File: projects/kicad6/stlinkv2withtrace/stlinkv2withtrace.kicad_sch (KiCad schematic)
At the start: 7 parts, among them J3 STLinkV2, U1 YAAJ_BluePill_Part_Like

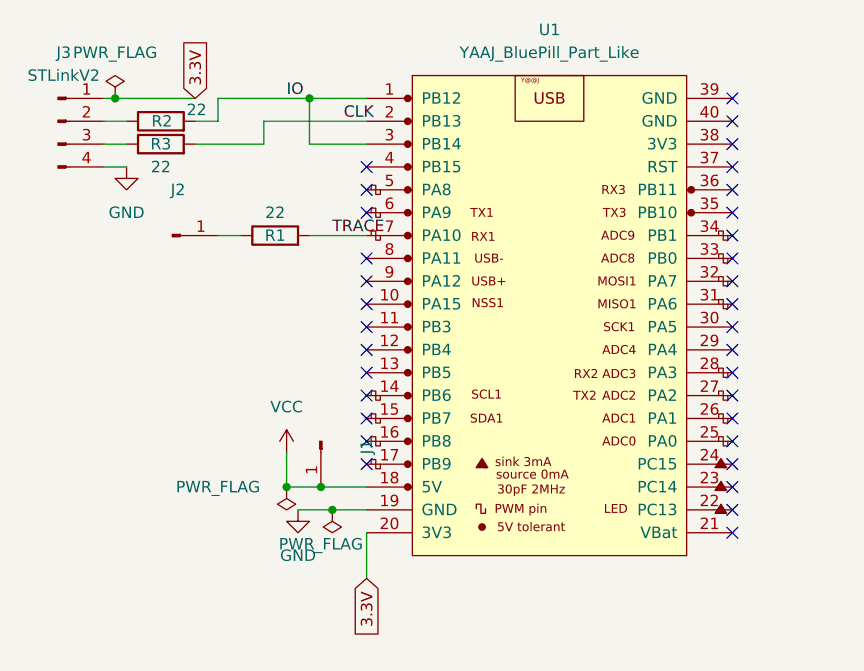
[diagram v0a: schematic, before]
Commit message: Add stlink v2 diy programmer
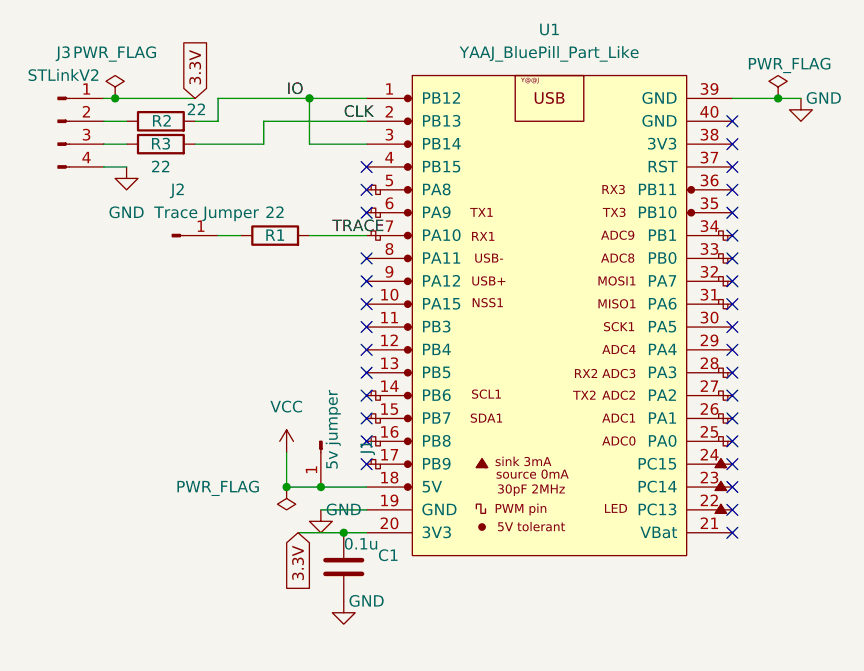
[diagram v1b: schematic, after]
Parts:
- added C1: 0.1u, Capacitor_THT:C_Axial_L3.8mm_D2.6mm_P7.50mm_Horizontal, symbol Device:C
- J1: value (none) -> 5v jumper
- J2: value (none) -> Trace Jumper; footprint (none) -> Connector_PinSocket_2.54mm:PinSocket_1x01_P2.54mm_Vertical
- J3: footprint (none) -> Connector_PinSocket_2.54mm:PinSocket_1x04_P2.54mm_Horizontal
- R1, R2, R3: footprint (none) -> Resistor_THT:R_Axial_DIN0207_L6.3mm_D2.5mm_P7.62mm_Horizontal
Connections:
- net 3.3V: now also C1.1
- net GND: now also U1.39 (GND), C1.2
- no-connect marks 33 -> 32
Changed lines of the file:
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@@
     (company "Amitesh Singh")
   )
-  (junction (at 116.84 110.49) (diameter 0) (color 0 0 0 0)
+  (junction (at 166.37 64.77) (diameter 0) (color 0 0 0 0)
   )
   (junction (at 114.3 64.77) (diameter 0) (color 0 0 0 0)
   )
   (junction (at 111.76 107.95) (diameter 0) (color 0 0 0 0)
+  )
+  (junction (at 118.11 113.03) (diameter 0) (color 0 0 0 0)
   )
   (junction (at 92.71 64.77) (diameter 0) (color 0 0 0 0)
@@
   (no_connect (at 120.65 77.47))
   (no_connect (at 120.65 82.55))
+  (no_connect (at 161.29 69.85))
   (no_connect (at 161.29 113.03))
   (no_connect (at 161.29 110.49))
@@
   (no_connect (at 161.29 85.09))
   (no_connect (at 161.29 72.39))
-  (no_connect (at 161.29 69.85))
   (no_connect (at 161.29 67.31))
-  (no_connect (at 161.29 64.77))
   (no_connect (at 161.29 77.47))
   (no_connect (at 161.29 80.01))
@@
     (stroke (width 0) (type default) (color 0 0 0 0))
   )
-  (wire (pts (xy 120.65 118.11) (xy 120.65 113.03))
+  (wire (pts (xy 115.57 110.49) (xy 120.65 110.49))
     (stroke (width 0) (type default) (color 0 0 0 0))
   )
@@
     (stroke (width 0) (type default) (color 0 0 0 0))
   )
+  (wire (pts (xy 161.29 64.77) (xy 166.37 64.77))
+    (stroke (width 0) (type default) (color 0 0 0 0))
+  )
   (wire (pts (xy 114.3 64.77) (xy 114.3 69.85))
     (stroke (width 0) (type default) (color 0 0 0 0))
@@
     (stroke (width 0) (type default) (color 0 0 0 0))
   )
-  (wire (pts (xy 113.03 110.49) (xy 116.84 110.49))
+  (wire (pts (xy 166.37 64.77) (xy 168.91 64.77))
+    (stroke (width 0) (type default) (color 0 0 0 0))
+  )
+  (wire (pts (xy 118.11 113.03) (xy 113.03 113.03))
     (stroke (width 0) (type default) (color 0 0 0 0))
   )
@@
     (stroke (width 0) (type default) (color 0 0 0 0))
   )
-  (wire (pts (xy 116.84 110.49) (xy 120.65 110.49))
+  (wire (pts (xy 120.65 113.03) (xy 118.11 113.03))
     (stroke (width 0) (type default) (color 0 0 0 0))
   )
@@
     )
   )
-  (global_label "3.3V" (shape input) (at 120.65 118.11 270) (fields_autoplaced)
+  (global_label "3.3V" (shape input) (at 113.03 113.03 270) (fields_autoplaced)
     (effects (font (size 1.27 1.27)) (justify right))
-    (property "Intersheet References" "${INTERSHEET_REFS}" (id 0) (at 120.5706 124.6355 90)
+    (property "Intersheet References" "${INTERSHEET_REFS}" (id 0) (at 112.9506 119.5555 90)
       (effects (font (size 1.27 1.27)) (justify right) hide)
     )
@@
     (pin "1")
   )
+  (symbol (lib_id "Device:C") (at 118.11 116.84 0) (unit 1)
+    (in_bom yes) (on_board yes)
+    (property "Reference" "C1" (id 0) (at 121.92 115.5699 0)
+      (effects (font (size 1.27 1.27)) (justify left))
+    )
+    (property "Value" "0.1u" (id 1) (at 118.11 114.3 0)
+      (effects (font (size 1.27 1.27)) (justify left))
+    )
+    (property "Footprint" "Capacitor_THT:C_Axial_L3.8mm_D2.6mm_P7.50mm_Horizontal" (id 2) (at 119.0752 120.65 0)
+      (effects (font (size 1.27 1.27)) hide)
+    )
+    (property "Datasheet" "~" (id 3) (at 118.11 116.84 0)
+      (effects (font (size 1.27 1.27)) hide)
+    )
+    (pin "1")
+    (pin "2")
+  )
   (symbol (lib_id "Device:R") (at 110.49 80.01 90) (unit 1)
     (in_bom yes) (on_board yes)
     (property "Reference" "R1" (id 0) (at 110.49 80.01 90))
     (property "Value" "22" (id 1) (at 110.49 77.47 90))
-    (property "Footprint" "" (id 2) (at 110.49 81.788 90)
+    (property "Footprint" "Resistor_THT:R_Axial_DIN0207_L6.3mm_D2.5mm_P7.62mm_Horizontal" (id 2) (at 110.49 81.788 90)
       (effects (font (size 1.27 1.27)) hide)
     )
@@
     (pin "1")
     (pin "2")
+  )
+  (symbol (lib_id "power:GND") (at 118.11 120.65 0) (unit 1)
+    (in_bom yes) (on_board yes)
+    (property "Reference" "#PWR04" (id 0) (at 118.11 127 0)
+      (effects (font (size 1.27 1.27)) hide)
+    )
+    (property "Value" "GND" (id 1) (at 120.65 120.65 0))
+    (property "Footprint" "" (id 2) (at 118.11 120.65 0)
+      (effects (font (size 1.27 1.27)) hide)
+    )
+    (property "Datasheet" "" (id 3) (at 118.11 120.65 0)
+      (effects (font (size 1.27 1.27)) hide)
+    )
+    (pin "1")
   )
   (symbol (lib_id "YAAJ_BlackPill_SWD_Breakout:YAAJ_BluePill_Part_Like") (at 140.97 87.63 0) (unit 1)
@@
       (effects (font (size 1.27 1.27)) (justify left))
     )
-    (property "Footprint" "" (id 2) (at 97.79 69.088 90)
+    (property "Footprint" "Resistor_THT:R_Axial_DIN0207_L6.3mm_D2.5mm_P7.62mm_Horizontal" (id 2) (at 97.79 69.088 90)
       (effects (font (size 1.27 1.27)) hide)
     )
@@
     (in_bom yes) (on_board yes)
     (property "Reference" "J1" (id 0) (at 120.65 103.505 0))
-    (property "Value" "" (id 1) (at 116.84 101.6 0))
+    (property "Value" "5v jumper" (id 1) (at 116.84 101.6 0))
     (property "Footprint" "Connector_PinSocket_2.54mm:PinSocket_1x01_P2.54mm_Vertical" (id 2) (at 115.57 102.87 0)
       (effects (font (size 1.27 1.27)) hide)
     )
     (property "Datasheet" "~" (id 3) (at 115.57 102.87 0)
+      (effects (font (size 1.27 1.27)) hide)
+    )
+    (pin "1")
+  )
+  (symbol (lib_id "power:GND") (at 115.57 110.49 0) (unit 1)
+    (in_bom yes) (on_board yes)
+    (property "Reference" "#PWR05" (id 0) (at 115.57 116.84 0)
+      (effects (font (size 1.27 1.27)) hide)
+    )
+    (property "Value" "GND" (id 1) (at 118.11 110.49 0))
+    (property "Footprint" "" (id 2) (at 115.57 110.49 0)
+      (effects (font (size 1.27 1.27)) hide)
+    )
+    (property "Datasheet" "" (id 3) (at 115.57 110.49 0)
       (effects (font (size 1.27 1.27)) hide)
     )
@@
     (in_bom yes) (on_board yes)
     (property "Reference" "J2" (id 0) (at 99.695 74.93 0))
-    (property "Value" "" (id 1) (at 102.87 77.47 0))
-    (property "Footprint" "" (id 2) (at 99.06 80.01 0)
+    (property "Value" "Trace Jumper" (id 1) (at 102.87 77.47 0))
+    (property "Footprint" "Connector_PinSocket_2.54mm:PinSocket_1x01_P2.54mm_Vertical" (id 2) (at 99.06 80.01 0)
       (effects (font (size 1.27 1.27)) hide)
     )
@@
     (property "Reference" "R3" (id 0) (at 97.79 69.85 90))
     (property "Value" "22" (id 1) (at 97.79 72.39 90))
-    (property "Footprint" "" (id 2) (at 97.79 71.628 90)
+    (property "Footprint" "Resistor_THT:R_Axial_DIN0207_L6.3mm_D2.5mm_P7.62mm_Horizontal" (id 2) (at 97.79 71.628 90)
       (effects (font (size 1.27 1.27)) hide)
     )
@@
     (property "Reference" "J3" (id 0) (at 86.995 59.69 0))
     (property "Value" "STLinkV2" (id 1) (at 86.995 62.23 0))
-    (property "Footprint" "" (id 2) (at 86.36 67.31 0)
+    (property "Footprint" "Connector_PinSocket_2.54mm:PinSocket_1x04_P2.54mm_Horizontal" (id 2) (at 86.36 67.31 0)
       (effects (font (size 1.27 1.27)) hide)
     )
@@
     (pin "4")
   )
-  (symbol (lib_id "power:GND") (at 113.03 110.49 0) (unit 1)
-    (in_bom yes) (on_board yes) (fields_autoplaced)
-    (property "Reference" "#PWR02" (id 0) (at 113.03 116.84 0)
-      (effects (font (size 1.27 1.27)) hide)
-    )
-    (property "Value" "GND" (id 1) (at 113.03 115.57 0))
-    (property "Footprint" "" (id 2) (at 113.03 110.49 0)
-      (effects (font (size 1.27 1.27)) hide)
-    )
-    (property "Datasheet" "" (id 3) (at 113.03 110.49 0)
+  (symbol (lib_id "power:GND") (at 168.91 64.77 0) (unit 1)
+    (in_bom yes) (on_board yes)
+    (property "Reference" "#PWR02" (id 0) (at 168.91 71.12 0)
+      (effects (font (size 1.27 1.27)) hide)
+    )
+    (property "Value" "GND" (id 1) (at 171.45 64.77 0))
+    (property "Footprint" "" (id 2) (at 168.91 64.77 0)
+      (effects (font (size 1.27 1.27)) hide)
+    )
+    (property "Datasheet" "" (id 3) (at 168.91 64.77 0)
       (effects (font (size 1.27 1.27)) hide)
     )
@@
     (pin "1")
   )
-  (symbol (lib_id "power:PWR_FLAG") (at 116.84 110.49 180) (unit 1)
-    (in_bom yes) (on_board yes)
-    (property "Reference" "#FLG02" (id 0) (at 116.84 112.395 0)
-      (effects (font (size 1.27 1.27)) hide)
-    )
-    (property "Value" "PWR_FLAG" (id 1) (at 115.57 114.3 0))
-    (property "Footprint" "" (id 2) (at 116.84 110.49 0)
-      (effects (font (size 1.27 1.27)) hide)
-    )
-    (property "Datasheet" "~" (id 3) (at 116.84 110.49 0)
+  (symbol (lib_id "power:PWR_FLAG") (at 166.37 64.77 0) (unit 1)
+    (in_bom yes) (on_board yes)
+    (property "Reference" "#FLG02" (id 0) (at 166.37 62.865 0)
+      (effects (font (size 1.27 1.27)) hide)
+    )
+    (property "Value" "PWR_FLAG" (id 1) (at 167.64 60.96 0))
+    (property "Footprint" "" (id 2) (at 166.37 64.77 0)
+      (effects (font (size 1.27 1.27)) hide)
+    )
+    (property "Datasheet" "~" (id 3) (at 166.37 64.77 0)
       (effects (font (size 1.27 1.27)) hide)
     )
@@
       (reference "#PWR03") (unit 1) (value "VCC") (footprint "")
     )
+    (path "/5dffeec2-7ab8-43ad-973e-743c383133b0"
+      (reference "#PWR04") (unit 1) (value "GND") (footprint "")
+    )
+    (path "/855e8331-3829-4dce-af2d-95c01e2d81c3"
+      (reference "#PWR05") (unit 1) (value "GND") (footprint "")
+    )
+    (path "/21f21aa6-0122-4e72-ae38-e4fc52e1755e"
+      (reference "C1") (unit 1) (value "0.1u") (footprint "Capacitor_THT:C_Axial_L3.8mm_D2.6mm_P7.50mm_Horizontal")
+    )
     (path "/6f243f53-6dea-48fd-9af8-df0adcc7c4d8"
       (reference "J1") (unit 1) (value "5v jumper") (footprint "Connector_PinSocket_2.54mm:PinSocket_1x01_P2.54mm_Vertical")
@@
     )
     (path "/a29f8df0-3fae-4edf-8d9c-bd5a875b13e3"
-      (reference "J3") (unit 1) (value "STLinkV2") (footprint "Connector_JST:JST_XA_B04B-XASK-1_1x04_P2.50mm_Vertical")
+      (reference "J3") (unit 1) (value "STLinkV2") (footprint "Connector_PinSocket_2.54mm:PinSocket_1x04_P2.54mm_Horizontal")
     )
     (path "/5549a117-8a09-4155-8430-af6adf42f74b"
